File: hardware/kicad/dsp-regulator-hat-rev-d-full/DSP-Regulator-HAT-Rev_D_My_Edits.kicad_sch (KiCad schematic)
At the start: 55 parts, among them J10 USB Hub I2C, J12 Conn_01x06_Pin, J17 JTAG, J18 Conn_01x04_Pin, J19 20021121-00010C4LF, J7 Fan, J8 Connector, USB-TYPE-C-16P, J9 Display Uart, Q9 AO3400A, U12 W25Q128, U13 AHT20, U15 AMS1117-3.3, U16 CH340C

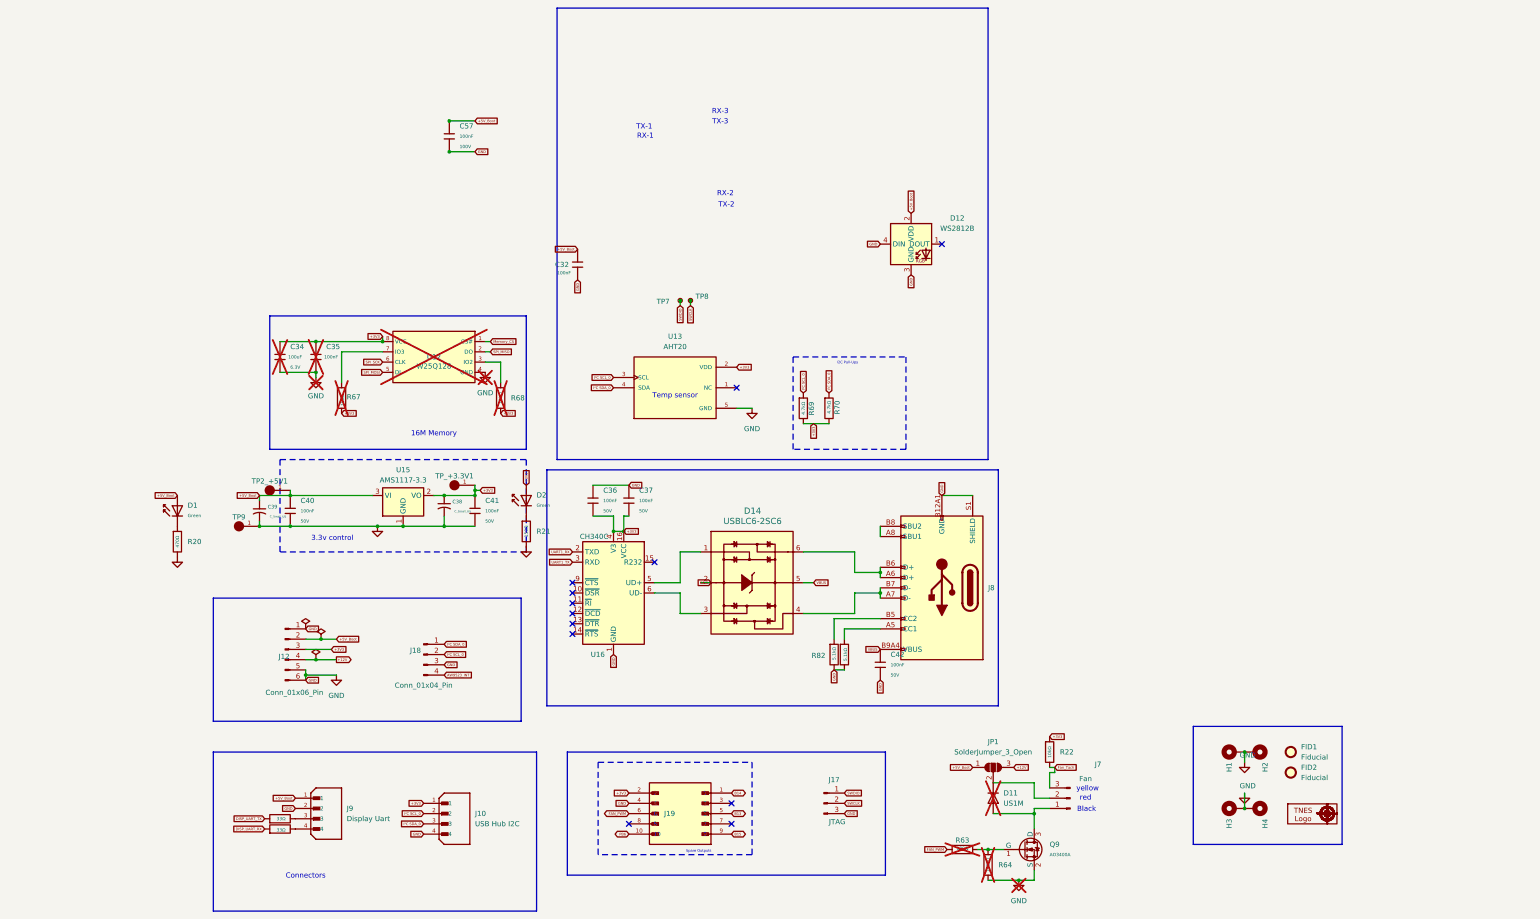
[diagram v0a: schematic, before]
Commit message: Preserve confirmed Rev-D My_Edits source set
Keep user-confirmed Rev-D My_Edits schematic/project/PCB in Git, preserve required project library tables, and add README provenance note with full SHA-256 hashes and report caveat.

Co-authored-by: Copilot <223556219+Copilot@users.noreply.github.com>
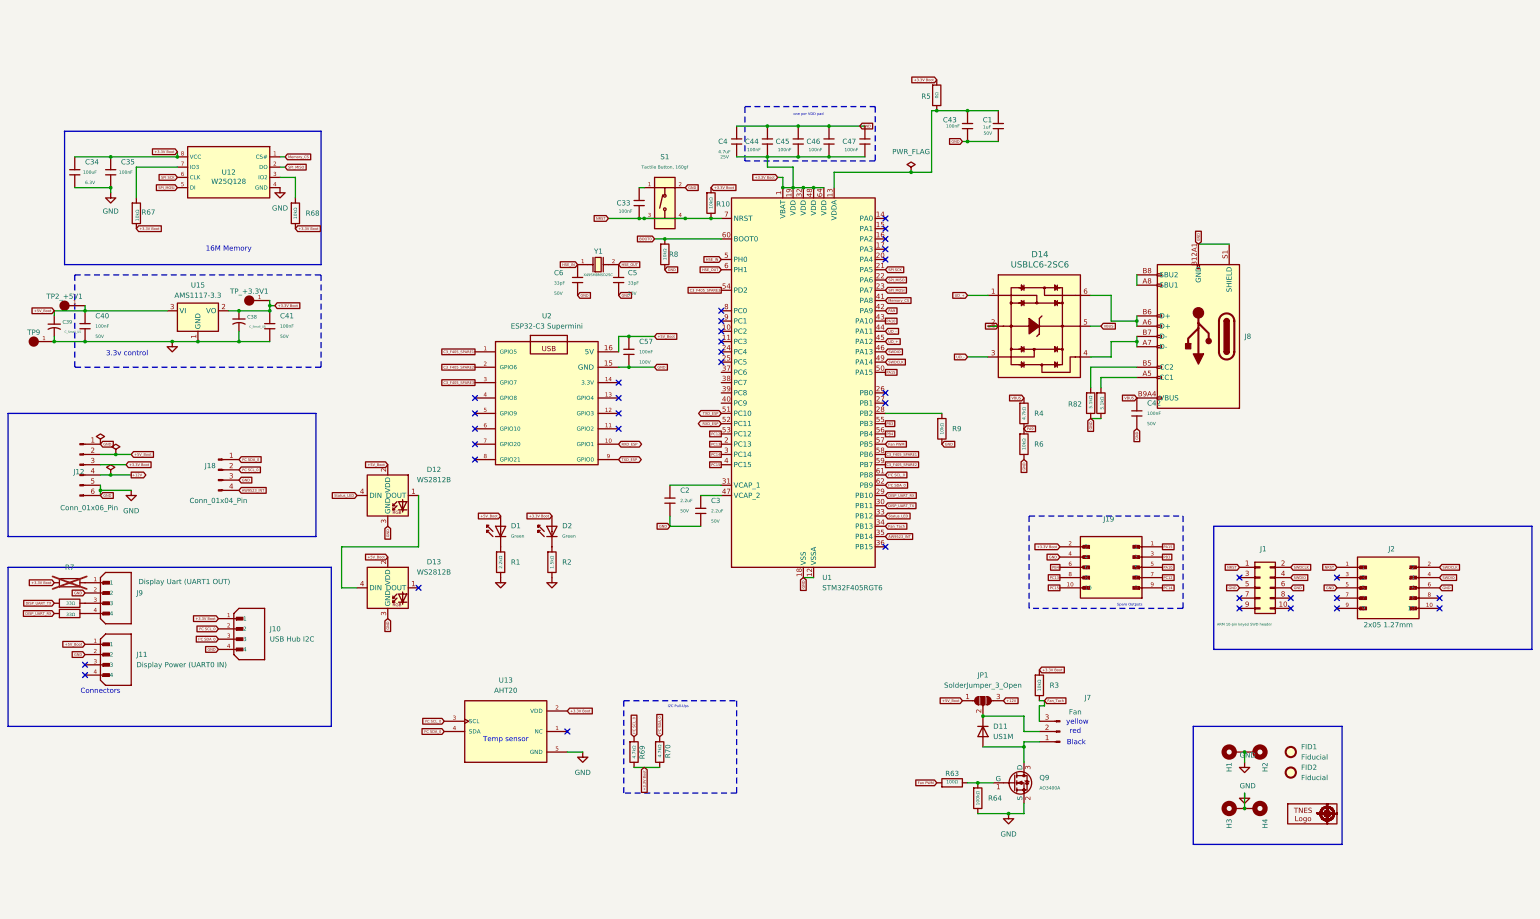
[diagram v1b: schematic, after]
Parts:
- removed C32, C36, C37: 100nF, PCM_JLCPCB:C_0805, symbol PCM_JLCPCB-Capacitors:0805,100nF,(2)
- removed J17: JTAG, Connector_PinHeader_2.54mm:PinHeader_1x03_P2.54mm_Vertical_SMD_Pin1Right, symbol Connector:Conn_01x03_Pin
- removed TP7, TP8: TestPoint_Small, Connector_PinHeader_1.00mm:PinHeader_1x01_P1.00mm_Vertical, symbol Connector:TestPoint_Small
- removed U16: CH340C, Package_SO:SOIC-16_3.9x9.9mm_P1.27mm, symbol 1My_IC's:CH340C
- added C1: 1uF, PCM_JLCPCB:C_0805, symbol PCM_JLCPCB-Capacitors:0805,1uF
- added C2, C3: 2.2uF, PCM_JLCPCB:C_0805, symbol PCM_JLCPCB-Capacitors:0805,2.2uF
- added C33, C43, C44, C45, C46, C47: 100nF, PCM_JLCPCB:C_0805, symbol PCM_JLCPCB-Capacitors:0805,100nF,(2)
- added C4: 4.7uF, PCM_JLCPCB:C_0805, symbol PCM_JLCPCB-Capacitors:0805,4.7uF
- added C5, C6: 33pF, PCM_JLCPCB:C_0805, symbol PCM_JLCPCB-Capacitors:0805,33pF
- added D13: WS2812B, PCM_JLCPCB:LED-SMD_4P-L1.6-W1.5_XL-1615RGBC-WS2812B, symbol PCM_JLCPCB-Extended:LED, WS2812B, 1615
- added J1: ARM 10-pin keyed SWD header, Connector_IDC:IDC-Header_2x05_P2.54mm_Vertical, symbol Connector_Generic:Conn_02x05_Odd_Even
- added J11: Display Power (UART0 IN), 1My_Parts_ Connectors:JST_B4B-XH-A, symbol 1My_Connectors:B4B-XH-A
- added J2: 2x05 1.27mm, digikey-footprints:PinHeader_2x5_P1.27mm, symbol 1My_Basic components:20021121-00010C4LF
- added R10, R6, R8, R9: 10kΩ, PCM_JLCPCB:R_0805, symbol PCM_JLCPCB-Resistors:0805,10kΩ
- added R4: 4.7kΩ, PCM_JLCPCB:R_0805, symbol PCM_JLCPCB-Resistors:0805,4.7kΩ
- added R5, R7: 0Ω, PCM_JLCPCB:R_0805, symbol PCM_JLCPCB-Resistors:0805,0Ω
- added S1: Tactile Button, 160gf, PCM_JLCPCB:SW-SMD_4P-L5.1-W5.1-P3.70-LS6.5-TL-2, symbol PCM_JLCPCB-Connectors_Buttons:Tactile Button, 160gf, 12V, 50mA, 5.1mm
- added U1: STM32F405RGT6, Package_QFP:LQFP-64_10x10mm_P0.5mm, symbol MCU_ST_STM32F4:STM32F405RGTx
- added U2: ESP32-C3 Supermini, SuperMini_Review:Teyleten_ESP32_C3_SuperMini, symbol 1My_MPUs:ESP32_C3__Super_Mini
- added Y1: X49SM8MSD2SC, PCM_JLCPCB:CRYSTAL-SMD_L11.5-W4.8-LS12.7, symbol PCM_JLCPCB-Crystals:Crystal, 8MHz, 20pF, ±20ppm
- C34, C35, D11, R63, R64, R67, R68, U12: now fitted
- J9: value Display Uart -> Display Uart (UART1 OUT)
- R1: renamed from R20; value 470Ω -> 2.2kΩ; symbol PCM_JLCPCB-Resistors:0805,470Ω -> PCM_JLCPCB-Resistors:0805,2.2kΩ; LCSC C17710 -> C17520; Part 0805W8F4700T5E -> 0805W8F2201T5E; Resistance 470Ω -> 2.2kΩ; Stock 931415 -> 1012630
- R2: renamed from R21; value 150Ω -> 1.5kΩ; symbol PCM_JLCPCB-Resistors:0805,150Ω -> PCM_JLCPCB-Resistors:0805,1.5kΩ; LCSC C17471 -> C4310; Part 0805W8F1500T5E -> 0805W8F1501T5E; Resistance 150Ω -> 1.5kΩ; Stock 290540 -> 447558
- renumbered R22 to R3
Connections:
- net +5V_Boot: now also D13.2 (VDD), J11.1, U2.16 (5V); no longer J9.1
- net AW9523_INT: now also U1.35 (PB14)
- net DISP_UART_RX: now also U1.29 (PB10)
- net DISP_UART_TX: now also U1.30 (PB11)
- net Fan_Tach: now also U1.34 (PB13)
- net GND: now also C1.1, C2.2, C3.2, C4.1, C43.2, C44.1, C45.1, C46.1, C47.1, C5.2, C6.2, D13.3 (GND), J1.5 (Pin_5), J1.6 (Pin_6), J11.2, J2.5, J2.6, R6.2, R8.2, R9.2, S1.2 (B), U1.12 (VSSA), U1.18 (VSS), U1.63 (VSS), U2.15 (GND); no longer D12.4 (DIN)
- net I²C SCL_0: now also U1.61 (PB8)
- net I²C SDA_0: now also U1.62 (PB9)
- net Memory_CS: now also U1.41 (PA8)
- net SPI_MISO: now also U1.22 (PA6)
- net SPI_MOSI: now also U1.23 (PA7)
- net SWDIO: now also J1.4 (Pin_4), J2.4, U1.46 (PA13)
- net VBUS: now also R4.1
- net UD_+: now reaches D14.1
- net UD_+: now also U1.45 (PA12)
- net UD_-: now reaches D14.3
- net UD_-: now also U1.44 (PA11)
- net PB3: now reaches J19.3
- net PB3: now also U1.55 (PB3)
- net PC12: now reaches J19.7
- net PC12: now also U1.53 (PC12)
- net PC13: now reaches J19.8
- net PC13: now also U1.2 (PC13)
- net at D12.1 (DOUT): now also D13.4 (DIN)
- net +3V3 renamed +3.3V Boot
- net +3.3V Boot: now also C4.2, C44.2, C45.2, C46.2, C47.2, R10.1, R5.1, R7.1, U1.1 (VBAT), U1.19 (VDD), U1.32 (VDD), U1.48 (VDD), U1.64 (VDD)
- net B13 renamed PA10
- net PA10: now also U1.43 (PA10)
- net B14 renamed PA15
- net PA15: now also U1.50 (PA15)
- net B15 renamed PC14
- net PC14: now also U1.3 (PC14)
- net FAN_PWM renamed Fan PWM
- net Fan PWM: now also U1.57 (PB5); no longer J19.6
- net PB6 renamed PC15
- net PC15: now also U1.4 (PC15)
- net SPI_SCK renamed SPI SCK
- net SPI SCK: now also U1.21 (PA5)
- new net: J9.1, R7.2
- new net: C2.1, U1.31 (VCAP_1)
- new net: C1.2, C43.1, R5.2, U1.13 (VDDA)
- new net: C33.1, S1.1 (A)
- new net: R9.1, U1.28 (PB2)
- new net: C3.1, U1.47 (VCAP_2)
- new net BOOT0: R8.1, U1.60 (BOOT0)
- new net C3_F405_SPARE1: U1.58 (PB6), U2.1 (GPIO5)
- new net C3_F405_SPARE2: U1.59 (PB7), U2.2 (GPIO6)
- new net C3_F405_SPARE3: U1.54 (PD2), U2.3 (GPIO7)
- new net HSE_IN: C6.1, U1.5 (PH0), Y1.1
- new net HSE_OUT: C5.1, U1.6 (PH1), Y1.2
- new net NRST: C33.2, J1.1 (Pin_1), J2.1, R10.2, S1.3 (C), S1.4 (D), U1.7 (NRST)
- new net PA9: R4.2, R6.1, U1.42 (PA9)
- new net PB4: J19.6, U1.56 (PB4)
- new net RXD_ESP: U1.52 (PC11), U2.10 (GPIO1)
- new net SWDCLK: J1.2 (Pin_2), J2.2, U1.49 (PA14)
- new net Status_LED: D12.4 (DIN), U1.33 (PB12)
- new net TXD_ESP: U1.51 (PC10), U2.9 (GPIO0)
- no-connect marks 12 -> 37
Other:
- note added: "one per VDD pad"
- note removed: "RX-1"
- note removed: "RX-2"
- note removed: "RX-3"
- note removed: "TX-1"
- note removed: "TX-2"
- note removed: "TX-3"
- title: DSP Regulator HAT Rev-D - selected Rev-C reuse -> DSP Regulator HAT
- moved on the sheet: C38, C39, C40, C41, C42, C57, D1, D12, D14, D2, J10, J12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
